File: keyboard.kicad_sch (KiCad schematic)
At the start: 20 parts, among them J2 Keyboard 1, J3 Keyboard 2, SW1 SW_Push, SW2 SW_Push, SW3 SW_Push, SW4 SW_Push, SW5 SW_Push, SW6 SW_Push

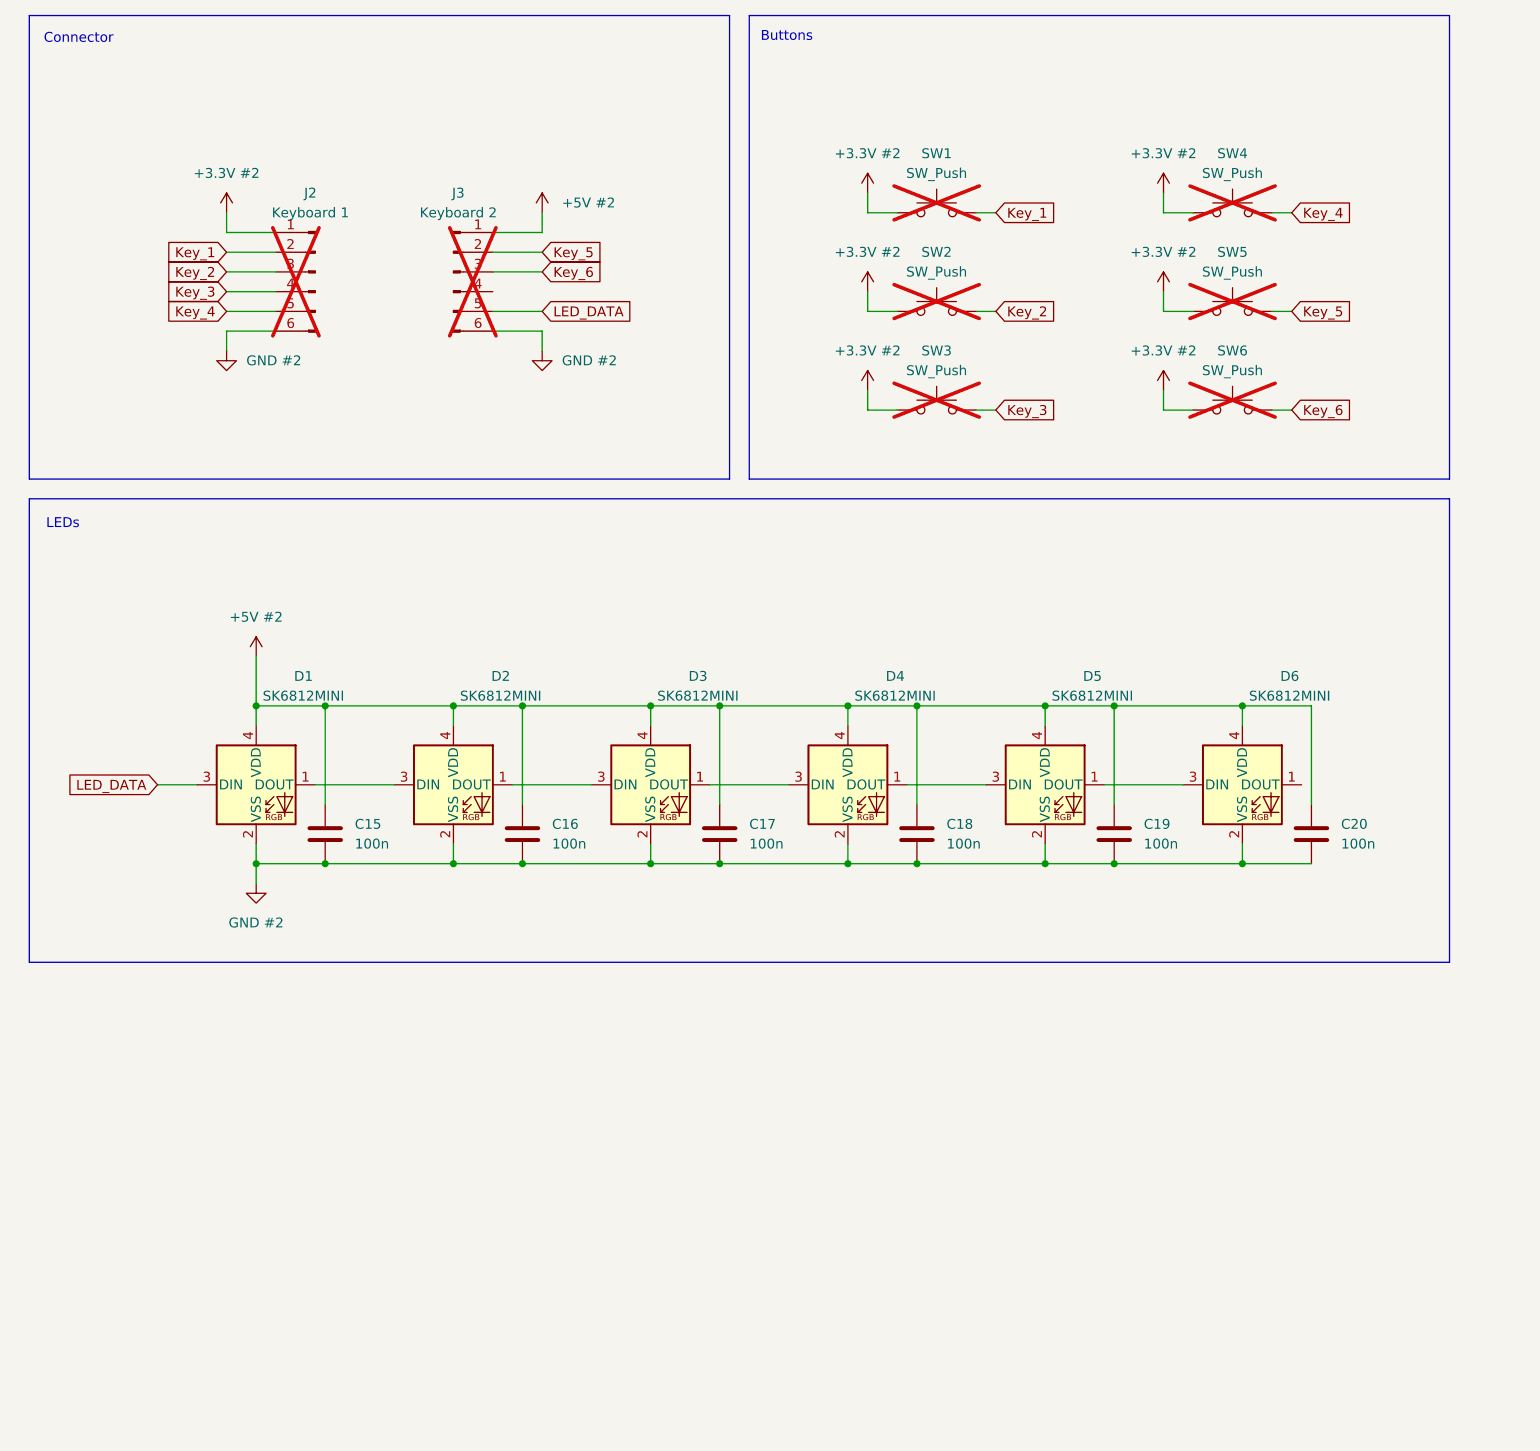
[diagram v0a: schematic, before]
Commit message: - Created head board tilable up to 4x - Placed and routed lines ToDo: - Print - I2C reanbable
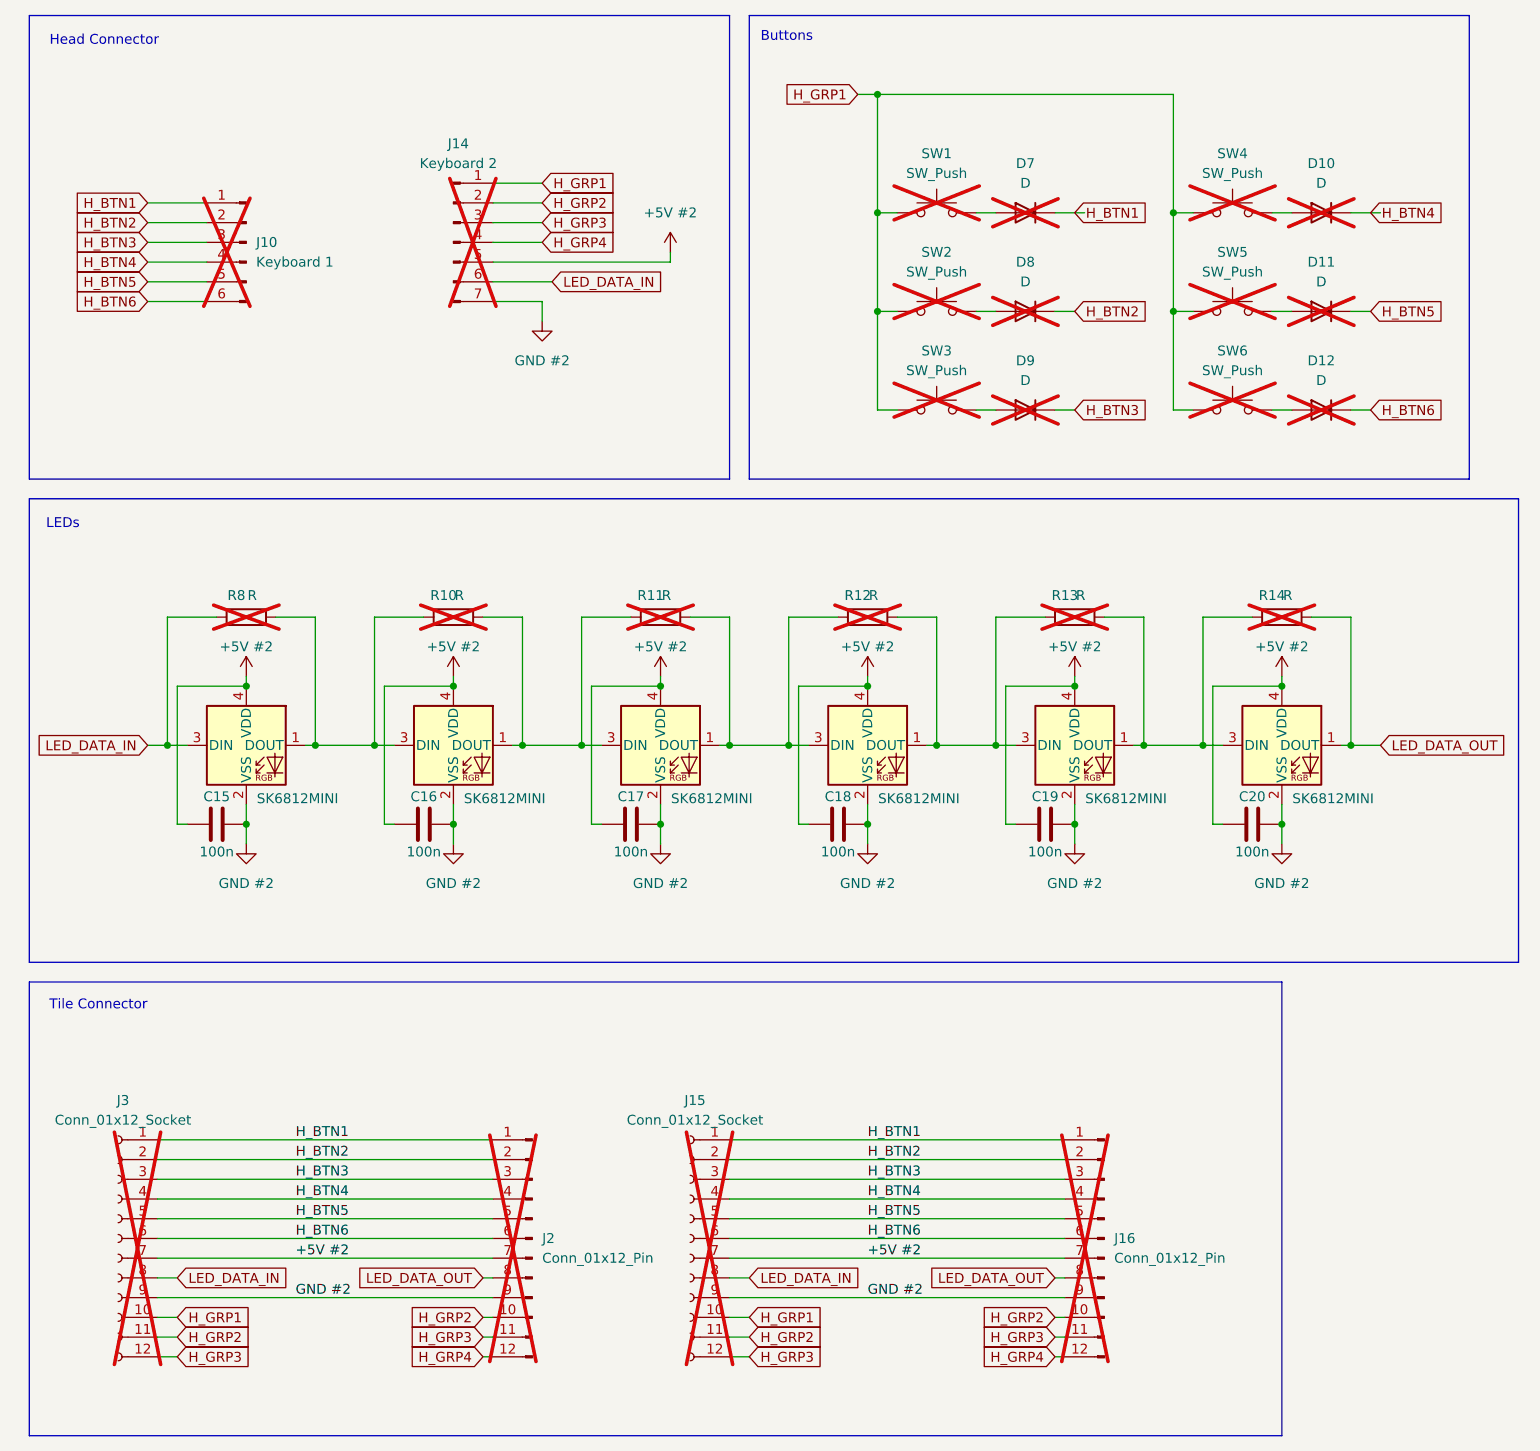
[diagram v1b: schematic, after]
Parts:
- removed J2: Keyboard 1, Connector_PinHeader_2.54mm:PinHeader_1x06_P2.54mm_Vertical, symbol Connector:Conn_01x06_Pin
- removed J3: Keyboard 2, Connector_PinHeader_2.54mm:PinHeader_1x06_P2.54mm_Vertical, symbol Connector:Conn_01x06_Pin
- added D10, D11, D12, D7, D8, D9: D, Diode_SMD:D_0603_1608Metric, symbol Device:D
- added J10: Keyboard 1, Connector_PinHeader_2.54mm:PinHeader_1x06_P2.54mm_Vertical, symbol Connector:Conn_01x06_Pin
- added J14: Keyboard 2, Connector_PinHeader_2.54mm:PinHeader_1x07_P2.54mm_Vertical, symbol Connector:Conn_01x07_Pin
- added J15, J3: Conn_01x12_Socket, Connector_PinSocket_2.54mm:PinSocket_1x12_P2.54mm_Horizontal, symbol Connector:Conn_01x12_Socket
- added J16, J2: Conn_01x12_Pin, Connector_PinHeader_2.54mm:PinHeader_1x12_P2.54mm_Horizontal, symbol Connector:Conn_01x12_Pin
- added R10, R11, R12, R13, R14, R8: R, Resistor_SMD:R_0603_1608Metric, symbol Device:R
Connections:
- net +5V #2: now also C15.2, C16.2, C17.2, C18.2, C19.2, C20.2, J14.5 (Pin_5), J15.7 (Pin_7), J16.7 (Pin_7), J2.7 (Pin_7), J3.7 (Pin_7); no longer C15.1, C16.1, C17.1, C18.1, C19.1, C20.1
- net GND #2: now also C15.1, C16.1, C17.1, C18.1, C19.1, C20.1, J14.7 (Pin_7), J15.9 (Pin_9), J16.9 (Pin_9), J2.9 (Pin_9), J3.9 (Pin_9); no longer C15.2, C16.2, C17.2, C18.2, C19.2, C20.2
- net at D4.1 (DOUT), D5.3 (DIN): now also R12.2, R13.1
- net at D3.1 (DOUT), D4.3 (DIN): now also R11.2, R12.1
- net at D5.1 (DOUT), D6.3 (DIN): now also R13.2, R14.1
- net at D2.1 (DOUT), D3.3 (DIN): now also R10.2, R11.1
- net at D1.1 (DOUT), D2.3 (DIN): now also R10.1, R8.2
- net LED_DATA_OUT: now reaches D6.1 (DOUT)
- net LED_DATA_OUT: now also J16.8 (Pin_8), J2.8 (Pin_8), R14.2
- net +3.3V #2 renamed H_GRP1
- net H_GRP1: now also J14.1 (Pin_1), J15.10 (Pin_10), J3.10 (Pin_10)
- net Key_1: no longer names the net of SW1.2
- net Key_1: now also D7.2 (A)
- net Key_2: no longer names the net of SW2.2
- net Key_2: now also D8.2 (A)
- net Key_3: no longer names the net of SW3.2
- net Key_3: now also D9.2 (A)
- net Key_4: no longer names the net of SW4.2
- net Key_4: now also D10.2 (A)
- net Key_5: no longer names the net of SW5.2
- net Key_5: now also D11.2 (A)
- net Key_6: no longer names the net of SW6.2
- net Key_6: now also D12.2 (A)
- net LED_DATA renamed LED_DATA_IN
- net LED_DATA_IN: now also J14.6 (Pin_6), J15.8 (Pin_8), J3.8 (Pin_8), R8.1
- new net H_BTN1: D7.1 (K), J10.1 (Pin_1), J15.1 (Pin_1), J16.1 (Pin_1), J2.1 (Pin_1), J3.1 (Pin_1)
- new net H_BTN2: D8.1 (K), J10.2 (Pin_2), J15.2 (Pin_2), J16.2 (Pin_2), J2.2 (Pin_2), J3.2 (Pin_2)
- new net H_BTN3: D9.1 (K), J10.3 (Pin_3), J15.3 (Pin_3), J16.3 (Pin_3), J2.3 (Pin_3), J3.3 (Pin_3)
- new net H_BTN4: D10.1 (K), J10.4 (Pin_4), J15.4 (Pin_4), J16.4 (Pin_4), J2.4 (Pin_4), J3.4 (Pin_4)
- new net H_BTN5: D11.1 (K), J10.5 (Pin_5), J15.5 (Pin_5), J16.5 (Pin_5), J2.5 (Pin_5), J3.5 (Pin_5)
- new net H_BTN6: D12.1 (K), J10.6 (Pin_6), J15.6 (Pin_6), J16.6 (Pin_6), J2.6 (Pin_6), J3.6 (Pin_6)
- new net H_GRP2: J14.2 (Pin_2), J15.11 (Pin_11), J16.10 (Pin_10), J2.10 (Pin_10), J3.11 (Pin_11)
- new net H_GRP3: J14.3 (Pin_3), J15.12 (Pin_12), J16.11 (Pin_11), J2.11 (Pin_11), J3.12 (Pin_12)
- new net H_GRP4: J14.4 (Pin_4), J16.12 (Pin_12), J2.12 (Pin_12)
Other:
- note added: "Head Connector"
- note added: "Tile Connector"
- note removed: "Connector"
- moved on the sheet: C15

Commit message: - Added missing library files to git - Added logo to silkscreen - ERC: Okay
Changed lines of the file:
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@@
-	(wire
-		(pts
-			(xy 146.05 39.37) (xy 149.86 39.37)
-		)
-		(stroke
-			(width 0)
-			(type default)
-		)
-	)
 	(wire
 		(pts
@@
 	(wire
 		(pts
+			(xy 184.15 39.37) (xy 186.69 39.37)
+		)
+		(stroke
+			(width 0)
+			(type default)
+		)
+	)
+	(wire
+		(pts
 			(xy 29.21 40.64) (xy 36.83 40.64)
 		)
@@
 	(wire
 		(pts
+			(xy 146.05 39.37) (xy 148.59 39.37)
+		)
+		(stroke
+			(width 0)
+			(type default)
+		)
+	)
+	(wire
+		(pts
 			(xy 139.7 100.33) (xy 139.7 118.11)
 		)
@@
 		)
 		(stroke
-			(width 0)
-			(type default)
-		)
-	)
-	(wire
-		(pts
-			(xy 184.15 39.37) (xy 187.96 39.37)
-		)
-		(stroke
